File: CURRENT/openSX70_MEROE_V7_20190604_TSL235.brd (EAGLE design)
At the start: 95.9 x 27.9 mm, 43 parts, among them J1 687106183722, Q1 5.8A/30V/35mΩ, Q2 5.8A/30V/35mΩ, U1 ATMEGA328P_TQFP, U2 TPS79501DCQ, Y1 CSTCE8M00G52Z-R0

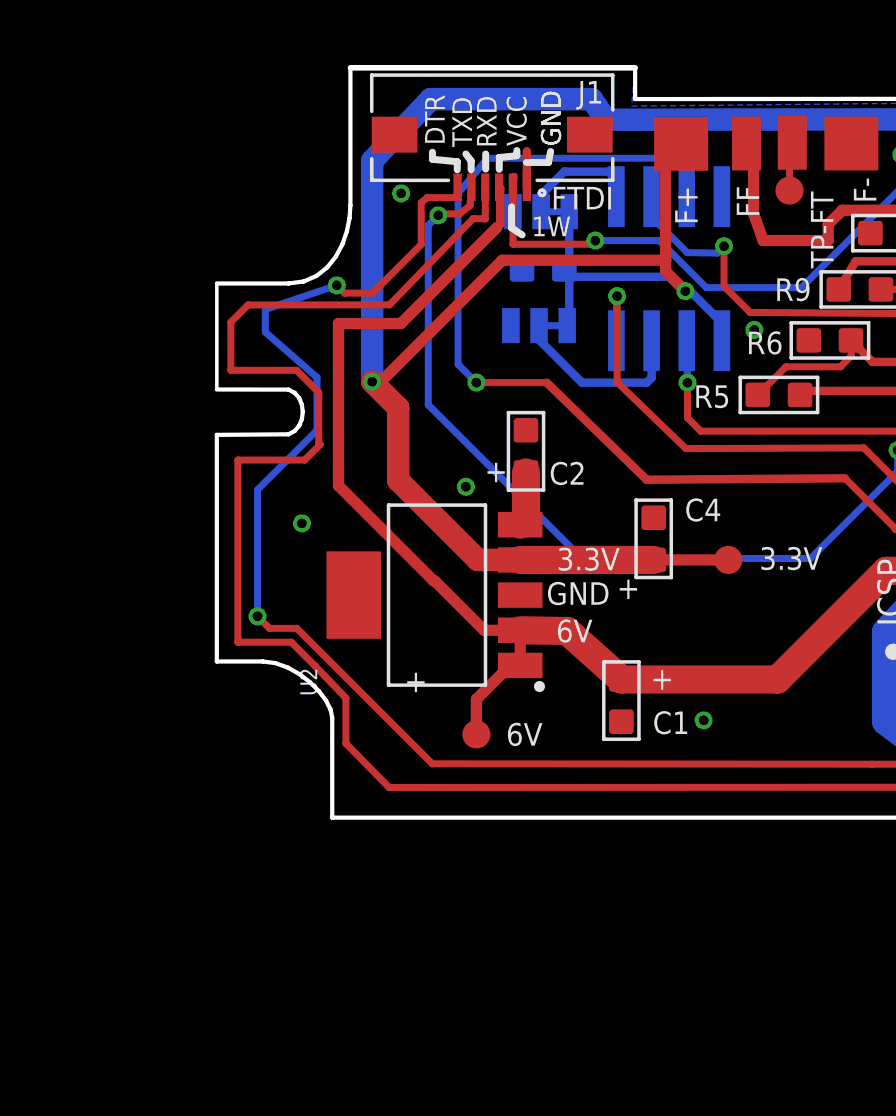
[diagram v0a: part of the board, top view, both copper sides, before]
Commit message: TSL235 test
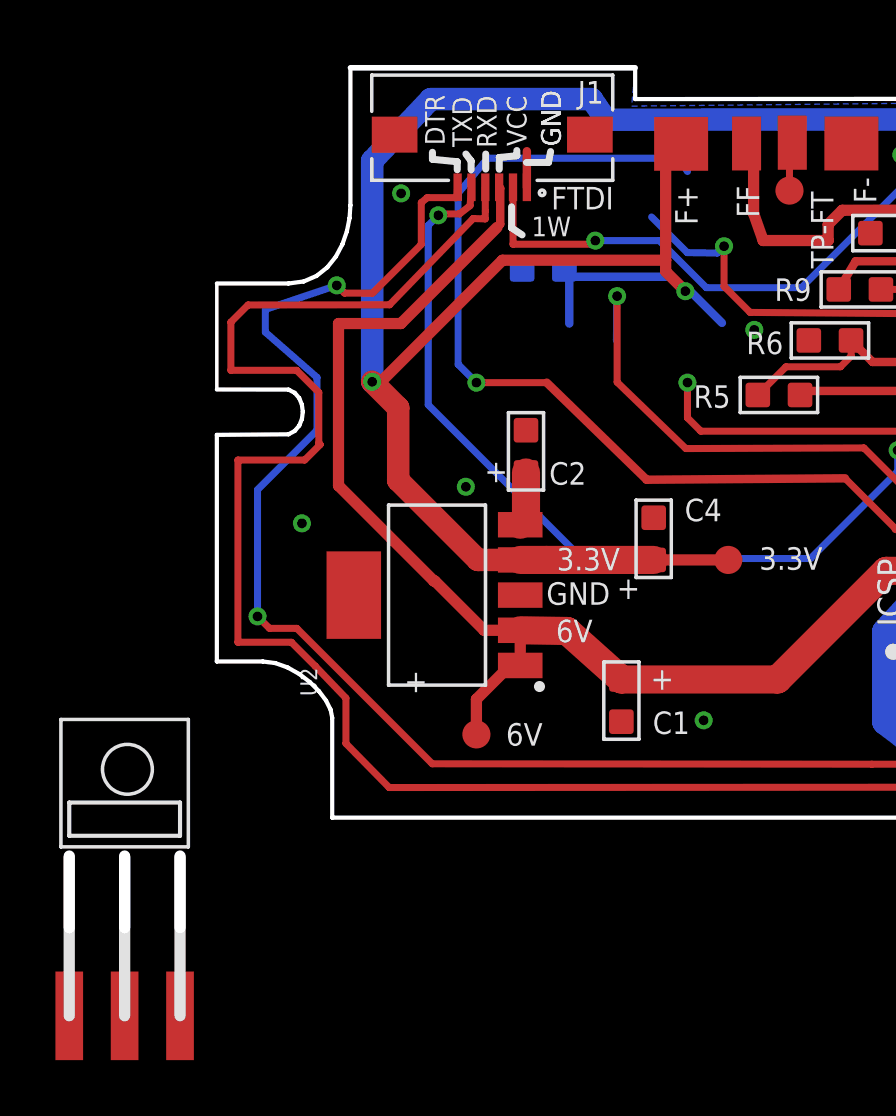
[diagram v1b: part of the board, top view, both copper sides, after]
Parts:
- removed S0: S0, SparkFun-Jumpers:SMT-JUMPER_3_1-NC_TRACE_SILK
- removed S2: S2, SparkFun-Jumpers:SMT-JUMPER_3_1-NC_TRACE_SILK
- removed TCS3200: TCS3200D, TCS3200D:SOIC8
- added U$3: TSL235R, _openSX70:TSL235R
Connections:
- removed net N$7: S0.2, TCS3200.1
- removed net N$8: S2.2, TCS3200.7
- net 3.3V: now also U$3.VDD; no longer S0.3, S2.3, TCS3200.5
- net GND: now also U$3.GND; no longer S0.1, S2.1, TCS3200.4
- net LM: now also U$3.OUT; no longer TCS3200.6
- net TCS3200_OE: no longer TCS3200.3
- net TCS3200_S1: no longer TCS3200.2
- net TCS3200_S3: no longer TCS3200.8
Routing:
- net N$8: track 6.62 -> 0.00 mm
- net N$7: track 4.41 -> 0.00 mm
- net 3.3V: track 159.8 -> 156.7 mm
- net LM: track 80.6 -> 79.1 mm
- net GND: track 6.15 -> 4.90 mm
- net TCS3200_OE: track 100.5 -> 99.6 mm
- net TCS3200_S1: track 73.9 -> 73.2 mm
